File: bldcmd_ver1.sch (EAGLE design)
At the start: 90 parts, among them CN1 DF61-2P-2.2V(23), CN2 DF65-3P-1.7V(21), CN3 SM04B-SRSS-TB, CN4 SM04B-SRSS-TB, CN5 SM05B-SRSS-TB, CN6 SM05B-SRSS-TB, IC1 STSPIN32F0A, IC2 AS5047P-ATSM, IC3 ADM4852ACPZ-REEL7, Q1 PSMN2R4-30MLD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

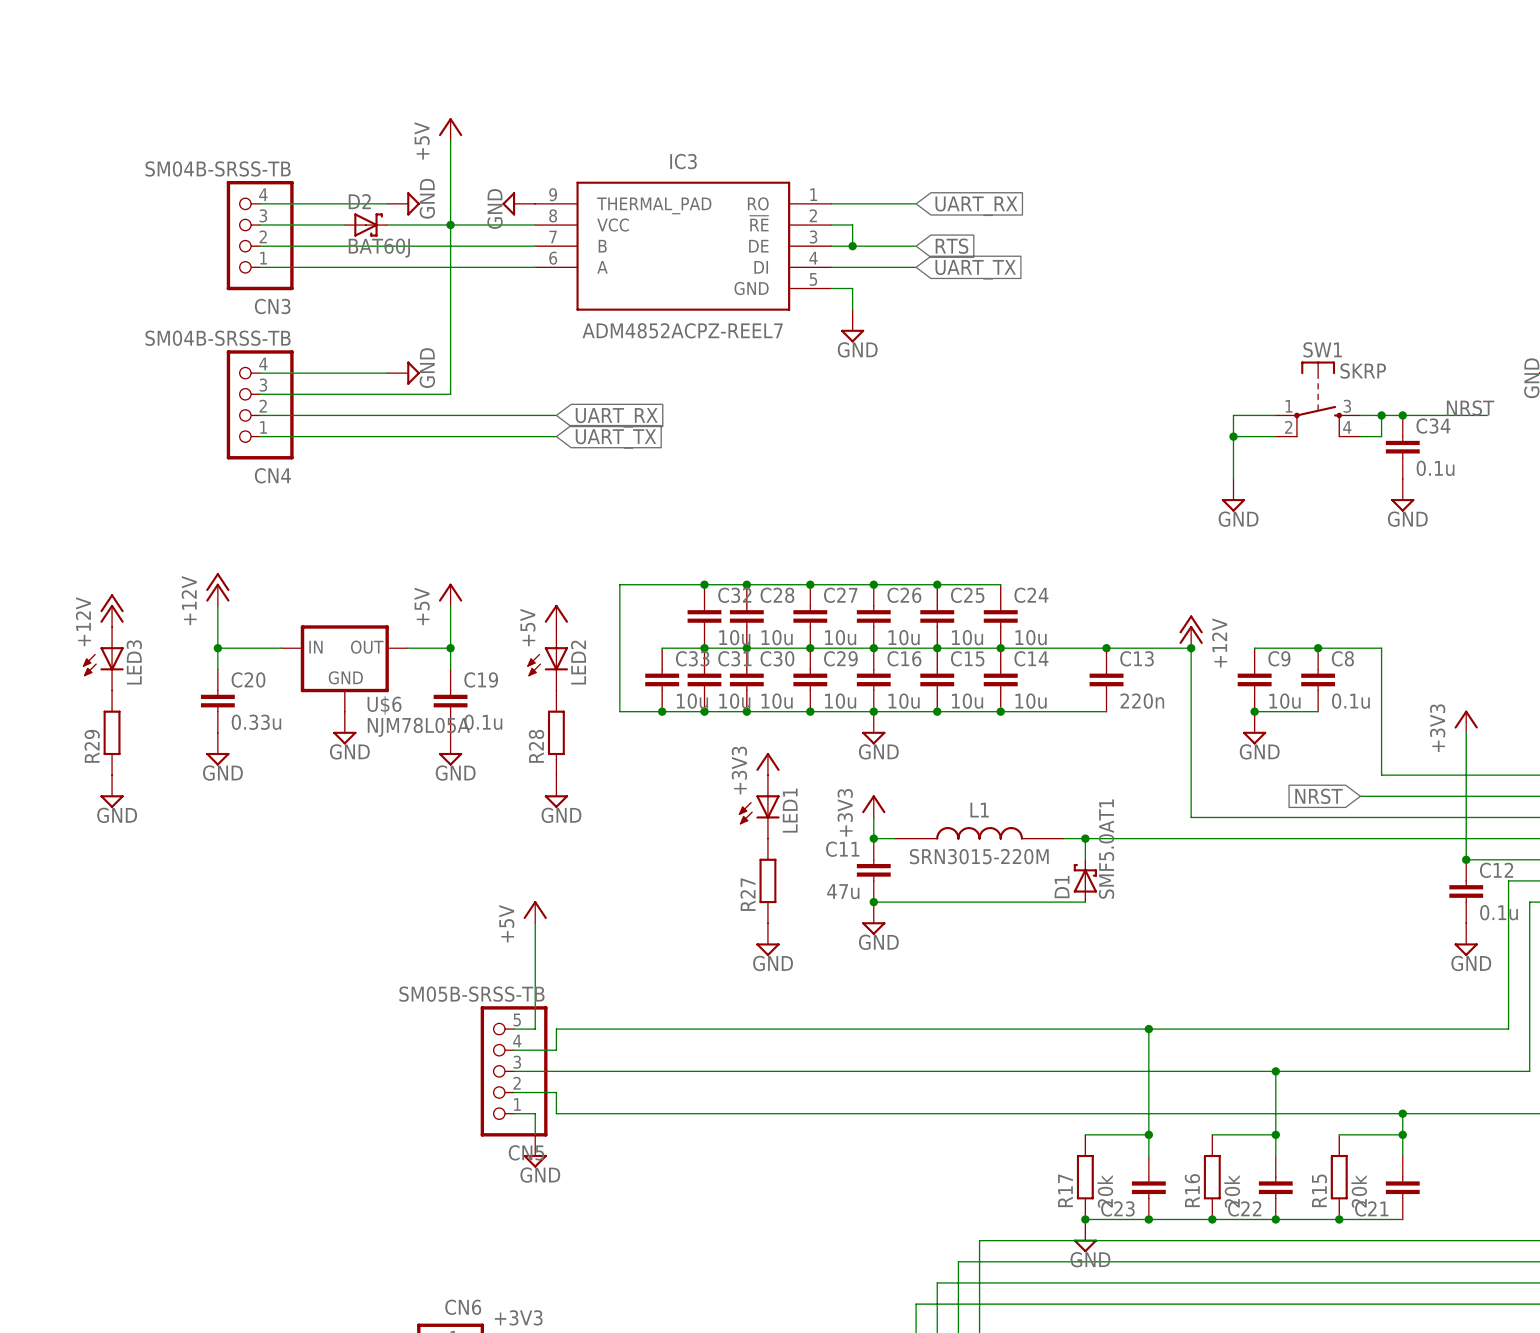
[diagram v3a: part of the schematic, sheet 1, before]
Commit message: 3端子レギュレータのライブラリ変更の反映 SHコネクタの接続順を反転
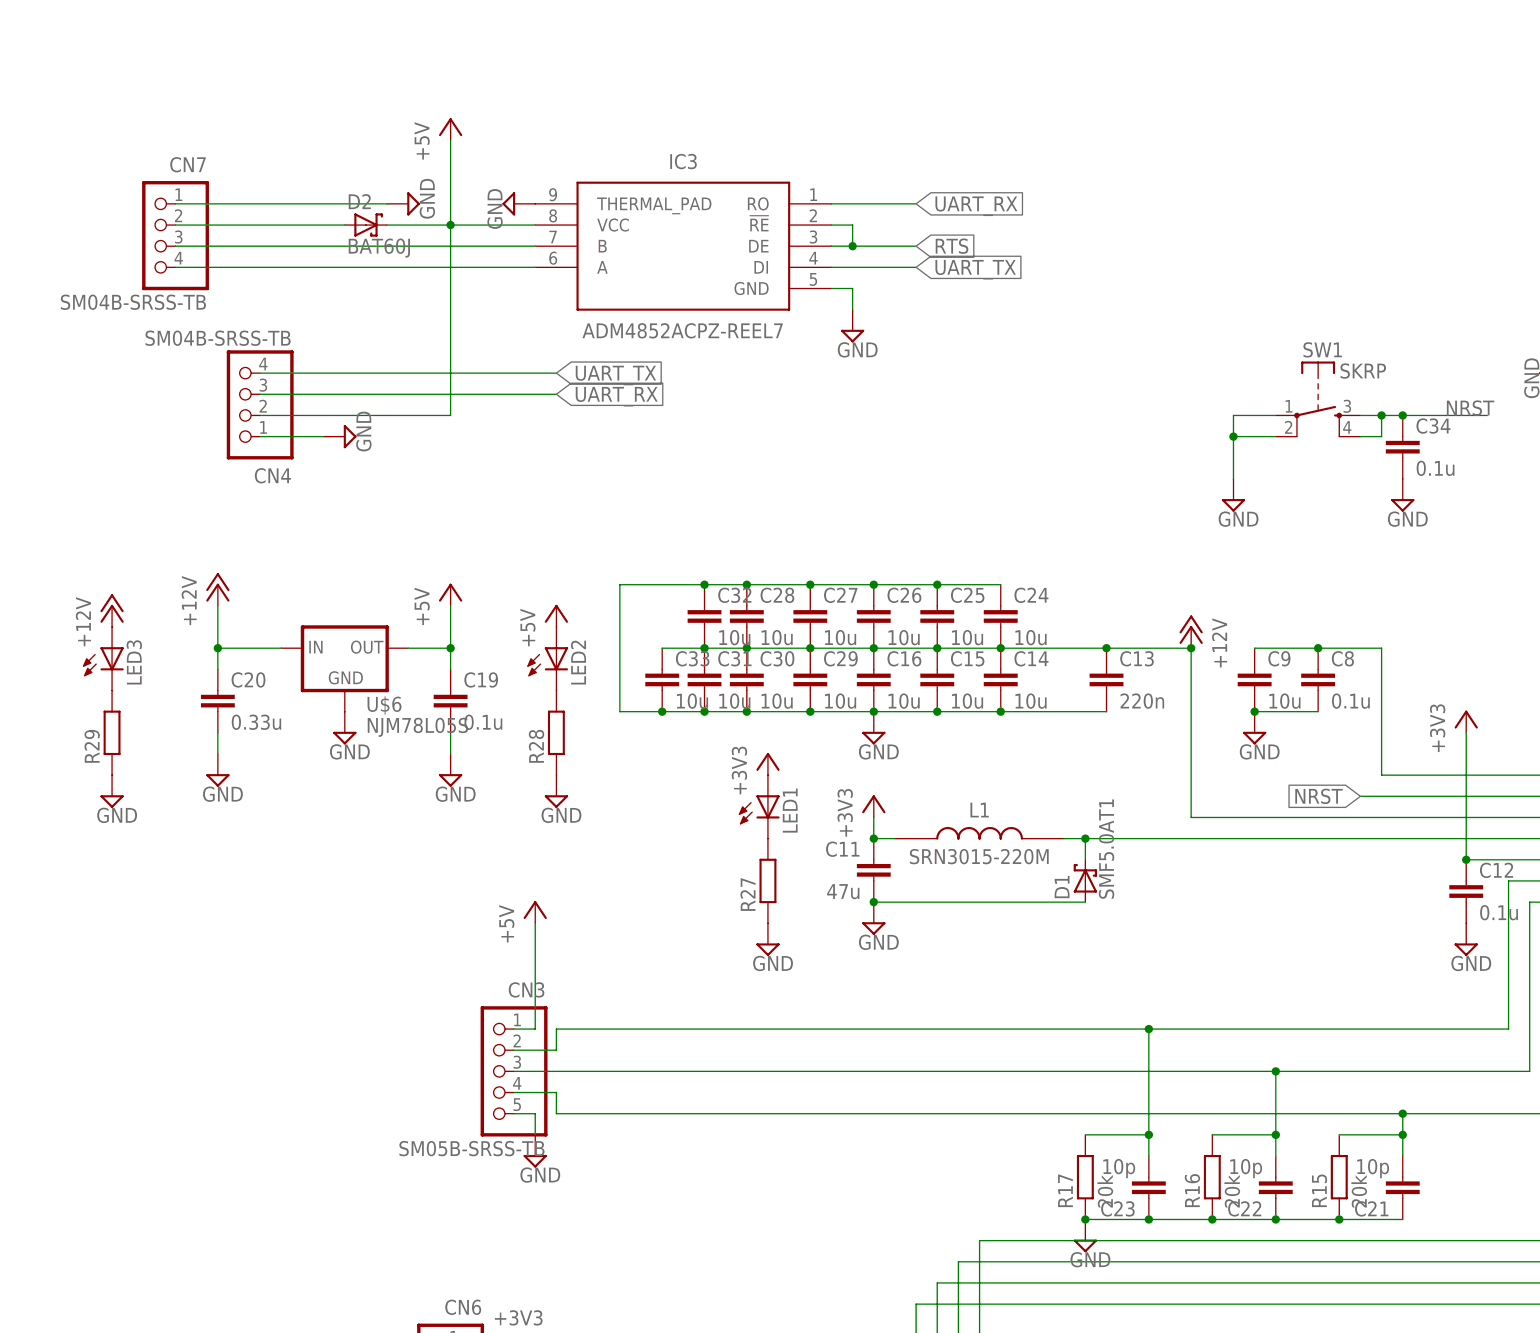
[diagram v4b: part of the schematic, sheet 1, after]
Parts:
- removed CN5: SM05B-SRSS-TB, scramble-con-jst:SM05B-SRSS-TB
- added CN7: SM04B-SRSS-TB, scramble-con-jst:SM04B-SRSS-TB
- C21, C22, C23: value (none) -> 10p
- CN3: value SM04B-SRSS-TB -> SM05B-SRSS-TB; device scramble-con-jst:SM04B-SRSS-TB -> scramble-con-jst:SM05B-SRSS-TB
- U$6: value NJM78L05A -> NJM78L05S; device rcssl_lib:NJM78L05A -> scramble-mcu:NJM78L05S
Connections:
- net +5V: now also CN3.1, CN4.2; no longer CN4.3, CN5.5
- net GND: now also CN3.5, CN4.1, CN7.1; no longer CN3.4, CN4.4, CN5.1
- net N$23: now also CN3.4; no longer CN5.2
- net N$24: now also CN3.3; no longer CN5.3
- net N$25: now also CN3.2; no longer CN5.4
- net N$29: now also CN7.3; no longer CN3.2
- net N$30: now also CN7.2; no longer CN3.3
- net N$32: now also CN7.4; no longer CN3.1
- net UART_RX: now also CN4.3; no longer CN4.2
- net UART_TX: now also CN4.4; no longer CN4.1

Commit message: 部品に必要な値を割り当てた，（最適なのか？） BOM出した
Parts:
- added D3: BAT60J, diode:BAT60J
- C1, C2, C3: value (none) -> 0.1u
- C17, C18: value (none) -> 100p
- L1: device rcssl_lib:SRN3015-220M -> scramble-mcu:SRN3015-220M
- R1, R2, R3, R4, R5, R6: value (none) -> 20
- R10, R11, R12, R29, R7, R8, R9: value (none) -> 10k
- R14, R26: value (none) -> 15k
- R21: value (none) -> NP
- R22, R24: value (none) -> 560
- R23: value (none) -> 8.2k
- R25, R27, R28: value (none) -> 1k
- renumbered CN4 to CN5
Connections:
- new net N$10: CN5.2, D3.A
- net +5V: now also D3.C; no longer CN5.2
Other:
- moved on the sheet: C17, CN7, D2, R14, R21

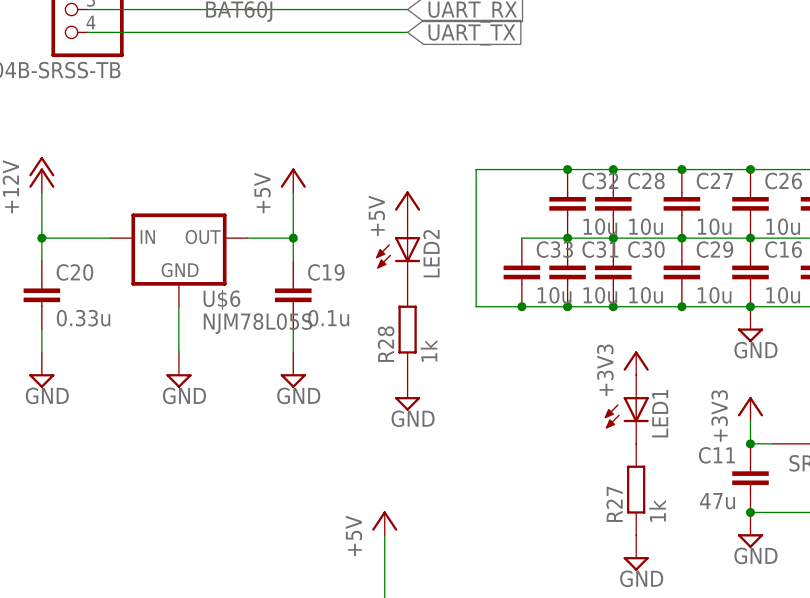
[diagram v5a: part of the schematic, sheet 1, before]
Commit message: AWを修正，コネクタの変更を適用
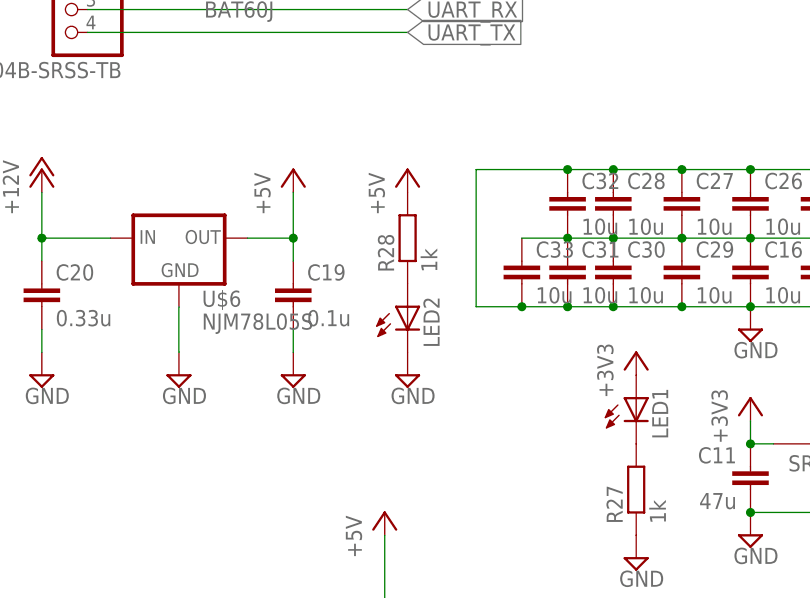
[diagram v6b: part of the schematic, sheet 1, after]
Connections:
- removed net N$33: LED2.C, R28.2
- new net N$21: LED2.A, R28.1
- net +5V: now also R28.2; no longer LED2.A
- net GND: now also LED2.C; no longer R28.1
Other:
- moved on the sheet: LED2, R28
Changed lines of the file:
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@@
 <?xml version="1.0" encoding="utf-8"?>
 <!DOCTYPE eagle SYSTEM "eagle.dtd">
-<eagle version="8.3.2">
+<eagle version="8.4.0">
 <drawing>
 <settings>
@@
 <grid distance="0.1" unitdist="inch" unit="inch" style="lines" multiple="1" display="no" altdistance="0.01" altunitdist="inch" altunit="inch"/>
 <layers>
-<layer number="1" name="Top" color="4" fill="1" visible="no" active="no"/>
-<layer number="2" name="Route2" color="1" fill="3" visible="no" active="no"/>
-<layer number="3" name="Route3" color="4" fill="3" visible="no" active="no"/>
-<layer number="4" name="Route4" color="1" fill="4" visible="no" active="no"/>
-<layer number="5" name="Route5" color="4" fill="4" visible="no" active="no"/>
-<layer number="6" name="Route6" color="1" fill="8" visible="no" active="no"/>
-<layer number="7" name="Route7" color="4" fill="8" visible="no" active="no"/>
-<layer number="8" name="Route8" color="1" fill="2" visible="no" active="no"/>
-<layer number="9" name="Route9" color="4" fill="2" visible="no" active="no"/>
-<layer number="10" name="Route10" color="1" fill="7" visible="no" active="no"/>
-<layer number="11" name="Route11" color="4" fill="7" visible="no" active="no"/>
-<layer number="12" name="Route12" color="1" fill="5" visible="no" active="no"/>
-<layer number="13" name="Route13" color="4" fill="5" visible="no" active="no"/>
-<layer number="14" name="Route14" color="1" fill="6" visible="no" active="no"/>
-<layer number="15" name="Route15" color="4" fill="6" visible="no" active="no"/>
-<layer number="16" name="Bottom" color="1" fill="1" visible="no" active="no"/>
-<layer number="17" name="Pads" color="2" fill="1" visible="no" active="no"/>
-<layer number="18" name="Vias" color="2" fill="1" visible="no" active="no"/>
-<layer number="19" name="Unrouted" color="6" fill="1" visible="no" active="no"/>
-<layer number="20" name="Dimension" color="24" fill="1" visible="no" active="no"/>
-<layer number="21" name="tPlace" color="15" fill="1" visible="no" active="no"/>
-<layer number="22" name="bPlace" color="7" fill="1" visible="no" active="no"/>
-<layer number="23" name="tOrigins" color="15" fill="1" visible="no" active="no"/>
-<layer number="24" name="bOrigins" color="15" fill="1" visible="no" active="no"/>
-<layer number="25" name="tNames" color="11" fill="7" visible="no" active="no"/>
-<layer number="26" name="bNames" color="13" fill="7" visible="no" active="no"/>
-<layer number="27" name="tValues" color="7" fill="1" visible="no" active="no"/>
-<layer number="28" name="bValues" color="7" fill="1" visible="no" active="no"/>
+<layer number="1" name="Top" color="4" fill="1" visible="yes" active="no"/>
+<layer number="2" name="Route2" color="1" fill="3" visible="yes" active="no"/>
+<layer number="3" name="Route3" color="4" fill="3" visible="yes" active="no"/>
+<layer number="4" name="Route4" color="1" fill="4" visible="yes" active="no"/>
+<layer number="5" name="Route5" color="4" fill="4" visible="yes" active="no"/>
+<layer number="6" name="Route6" color="1" fill="8" visible="yes" active="no"/>
+<layer number="7" name="Route7" color="4" fill="8" visible="yes" active="no"/>
+<layer number="8" name="Route8" color="1" fill="2" visible="yes" active="no"/>
+<layer number="9" name="Route9" color="4" fill="2" visible="yes" active="no"/>
+<layer number="10" name="Route10" color="1" fill="7" visible="yes" active="no"/>
+<layer number="11" name="Route11" color="4" fill="7" visible="yes" active="no"/>
+<layer number="12" name="Route12" color="1" fill="5" visible="yes" active="no"/>
+<layer number="13" name="Route13" color="4" fill="5" visible="yes" active="no"/>
+<layer number="14" name="Route14" color="1" fill="6" visible="yes" active="no"/>
+<layer number="15" name="Route15" color="4" fill="6" visible="yes" active="no"/>
+<layer number="16" name="Bottom" color="1" fill="1" visible="yes" active="no"/>
+<layer number="17" name="Pads" color="2" fill="1" visible="yes" active="no"/>
+<layer number="18" name="Vias" color="2" fill="1" visible="yes" active="no"/>
+<layer number="19" name="Unrouted" color="6" fill="1" visible="yes" active="no"/>
+<layer number="20" name="Dimension" color="24" fill="1" visible="yes" active="no"/>
+<layer number="21" name="tPlace" color="31" fill="10" visible="yes" active="no"/>
+<layer number="22" name="bPlace" color="25" fill="10" visible="yes" active="no"/>
+<layer number="23" name="tOrigins" color="15" fill="1" visible="yes" active="no"/>
+<layer number="24" name="bOrigins" color="15" fill="1" visible="yes" active="no"/>
+<layer number="25" name="tNames" color="11" fill="7" visible="yes" active="no"/>
+<layer number="26" name="bNames" color="13" fill="7" visible="yes" active="no"/>
+<layer number="27" name="tValues" color="7" fill="1" visible="yes" active="no"/>
+<layer number="28" name="bValues" color="7" fill="1" visible="yes" active="no"/>
 <layer number="29" name="tStop" color="7" fill="3" visible="no" active="no"/>
 <layer number="30" name="bStop" color="7" fill="6" visible="no" active="no"/>
@@
 <layer number="35" name="tGlue" color="7" fill="4" visible="no" active="no"/>
 <layer number="36" name="bGlue" color="7" fill="5" visible="no" active="no"/>
-<layer number="37" name="tTest" color="7" fill="1" visible="no" active="no"/>
-<layer number="38" name="bTest" color="7" fill="1" visible="no" active="no"/>
+<layer number="37" name="tTest" color="7" fill="1" visible="yes" active="no"/>
+<layer number="38" name="bTest" color="7" fill="1" visible="yes" active="no"/>
 <layer number="39" name="tKeepout" color="4" fill="11" visible="no" active="no"/>
 <layer number="40" name="bKeepout" color="1" fill="11" visible="no" active="no"/>
@@
 <layer number="44" name="Drills" color="7" fill="1" visible="no" active="no"/>
 <layer number="45" name="Holes" color="7" fill="1" visible="no" active="no"/>
-<layer number="46" name="Milling" color="3" fill="1" visible="no" active="no"/>
-<layer number="47" name="Measures" color="7" fill="1" visible="no" active="no"/>
-<layer number="48" name="Document" color="7" fill="1" visible="no" active="no"/>
-<layer number="49" name="Reference" color="7" fill="1" visible="no" active="no"/>
-<layer number="50" name="dxf" color="7" fill="1" visible="no" active="no"/>
-<layer number="51" name="tDocu" color="14" fill="1" visible="no" active="no"/>
-<layer number="52" name="bDocu" color="11" fill="1" visible="no" active="no"/>
-<layer number="53" name="tGND_GNDA" color="7" fill="1" visible="no" active="no"/>
-<layer number="54" name="bGND_GNDA" color="7" fill="1" visible="no" active="no"/>
-<layer number="56" name="wert" color="7" fill="1" visible="no" active="no"/>
+<layer number="46" name="Milling" color="3" fill="1" visible="yes" active="no"/>
+<layer number="47" name="Measures" color="7" fill="1" visible="yes" active="no"/>
+<layer number="48" name="Document" color="7" fill="1" visible="yes" active="no"/>
+<layer number="49" name="Reference" color="7" fill="1" visible="yes" active="no"/>
+<layer number="50" name="dxf" color="7" fill="1" visible="yes" active="no"/>
+<layer number="51" name="tDocu" color="14" fill="1" visible="yes" active="no"/>
+<layer number="52" name="bDocu" color="11" fill="1" visible="yes" active="no"/>
+<layer number="53" name="tGND_GNDA" color="7" fill="1" visible="yes" active="no"/>
+<layer number="54" name="bGND_GNDA" color="7" fill="1" visible="yes" active="no"/>
+<layer number="56" name="wert" color="7" fill="1" visible="yes" active="no"/>
 <layer number="90" name="Modules" color="5" fill="1" visible="yes" active="yes"/>
 <layer number="91" name="Nets" color="2" fill="1" visible="yes" active="yes"/>
@@
 <instance part="+3V9" gate="G$1" x="-86.36" y="-10.16"/>
 <instance part="LED1" gate="G$1" x="-86.36" y="-15.24"/>
-<instance part="LED2" gate="G$1" x="-111.76" y="2.54"/>
+<instance part="LED2" gate="G$1" x="-111.76" y="-5.08"/>
 <instance part="LED3" gate="G$1" x="-165.1" y="2.54"/>
 <instance part="R27" gate="G$1" x="-86.36" y="-25.4" rot="R90"/>
-<instance part="R28" gate="G$1" x="-111.76" y="-7.62" rot="R90"/>
+<instance part="R28" gate="G$1" x="-111.76" y="2.54" rot="R90"/>
 <instance part="R29" gate="G$1" x="-165.1" y="-7.62" rot="R90"/>
 <instance part="SUPPLY25" gate="GND" x="-165.1" y="-15.24"/>
-<instance part="SUPPLY26" gate="GND" x="-111.76" y="-15.24"/>
+<instance part="SUPPLY26" gate="GND" x="-111.76" y="-12.7"/>
 <instance part="SUPPLY27" gate="GND" x="-86.36" y="-33.02"/>
-<instance part="P+8" gate="1" x="-111.76" y="7.62"/>
+<instance part="P+8" gate="1" x="-111.76" y="10.16"/>
 <instance part="P+9" gate="1" x="-165.1" y="7.62"/>
 <instance part="U$6" gate="G$1" x="-137.16" y="2.54"/>
@@
 </segment>
 <segment>
-<pinref part="R28" gate="G$1" pin="1"/>
-<pinref part="SUPPLY26" gate="GND" pin="GND"/>
-</segment>
-<segment>
 <pinref part="R27" gate="G$1" pin="1"/>
 <pinref part="SUPPLY27" gate="GND" pin="GND"/>
@@
 <wire x1="-147.32" y1="33.02" x2="-142.24" y2="33.02" width="0.1524" layer="91"/>
 <pinref part="CN5" gate="G$1" pin="1"/>
+</segment>
+<segment>
+<pinref part="LED2" gate="G$1" pin="C"/>
+<pinref part="SUPPLY26" gate="GND" pin="GND"/>
 </segment>
 </net>
@@
 </segment>
 <segment>
-<pinref part="LED2" gate="G$1" pin="A"/>
 <pinref part="P+8" gate="1" pin="+5V"/>
+<pinref part="R28" gate="G$1" pin="2"/>
 </segment>
 </net>
@@
 <pinref part="LED1" gate="G$1" pin="C"/>
 <pinref part="R27" gate="G$1" pin="2"/>
-</segment>
-</net>
-<net name="N$33" class="0">
-<segment>
-<pinref part="LED2" gate="G$1" pin="C"/>
-<pinref part="R28" gate="G$1" pin="2"/>
 </segment>
 </net>
@@
 </segment>
 </net>
+<net name="N$21" class="0">
+<segment>
+<pinref part="R28" gate="G$1" pin="1"/>
+<pinref part="LED2" gate="G$1" pin="A"/>
+</segment>
+</net>
